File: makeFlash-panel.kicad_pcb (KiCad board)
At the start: 2 copper layers, 100.1 x 78.7 mm, 34 parts, among them Q1 2N3904, Q2 2N3904

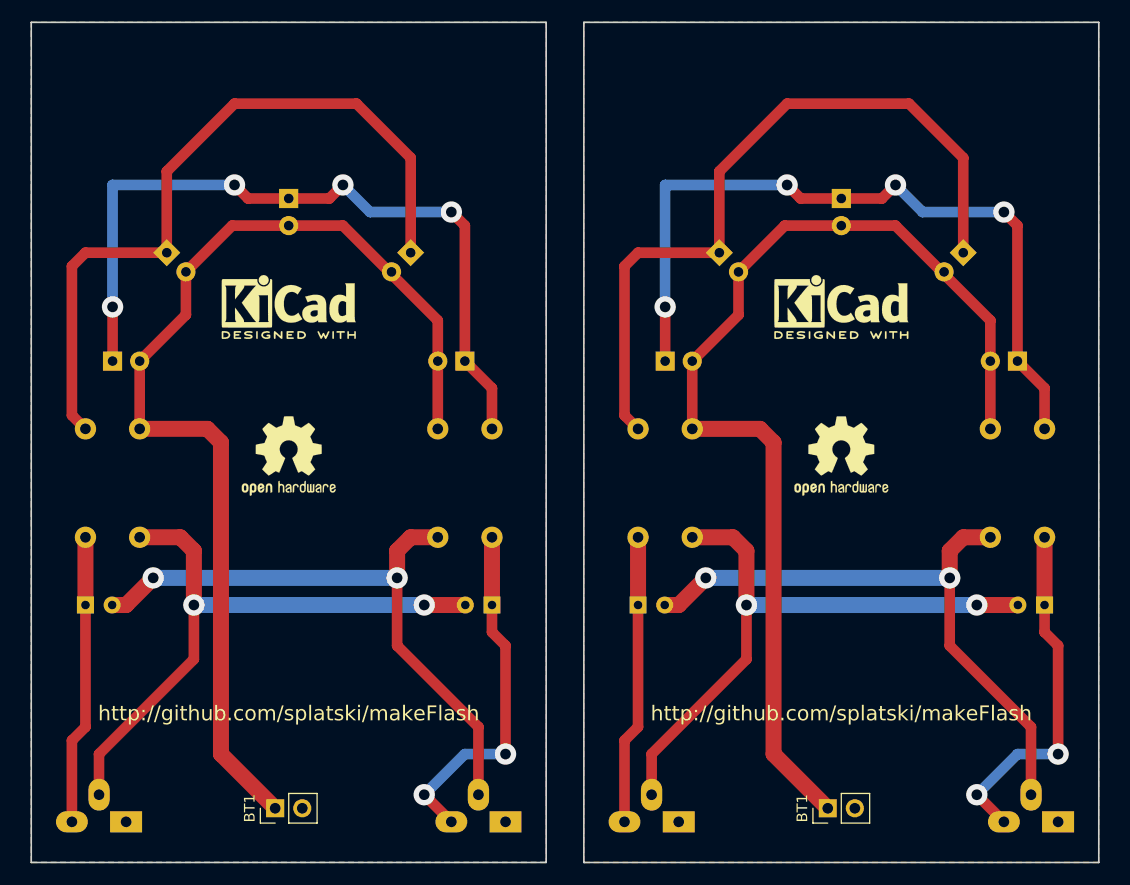
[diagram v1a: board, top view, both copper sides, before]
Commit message: slight reduction in size to definately fit within 100mm
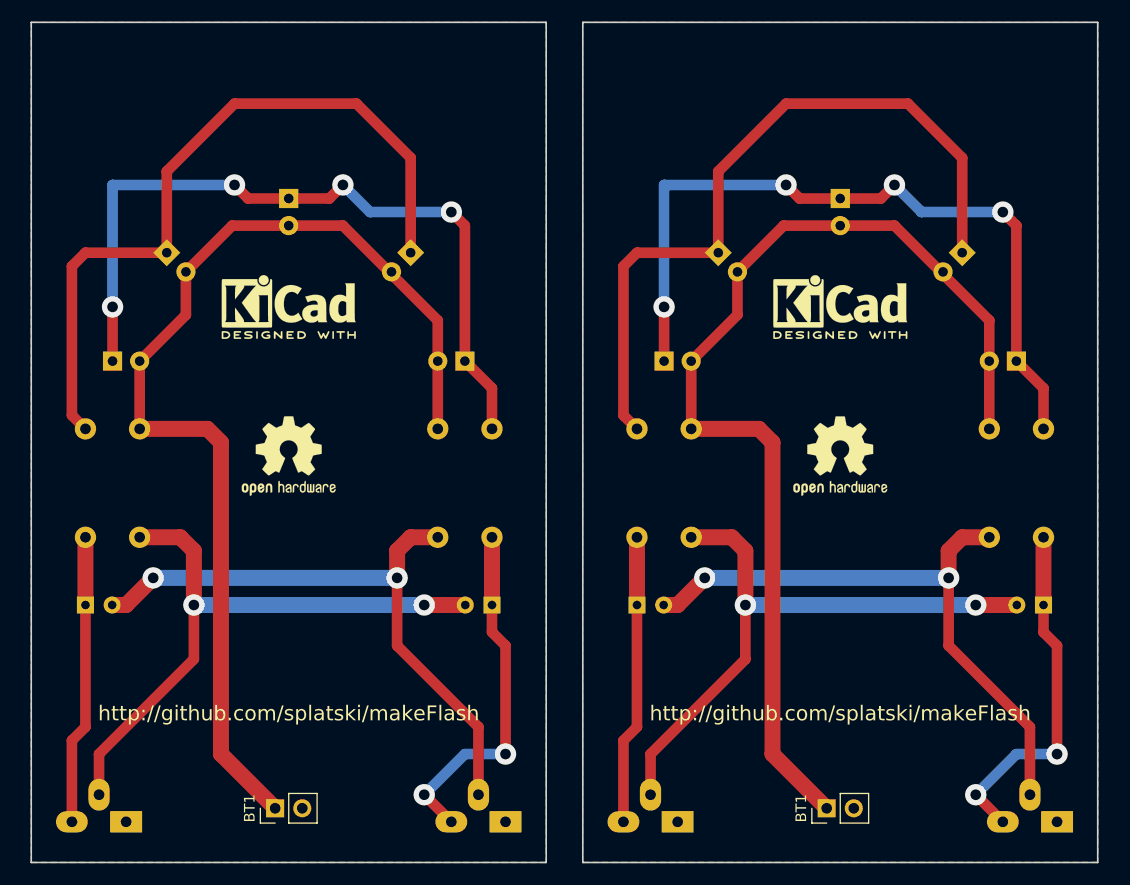
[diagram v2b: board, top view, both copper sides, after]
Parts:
- moved D3 0.10 mm to (136.8, 115.6)
- moved G*** 0.10 mm to (136.8, 133.3)
- moved KiCadLogo 0.10 mm to (136.8, 125.7)
- moved R4 0.10 mm to (150.8, 137.2)
- moved REF*** 0.10 mm to (136.8, 139.7)
- moved D1 0.10 mm to (120.3, 130.8)
- moved D2 0.10 mm to (125.4, 120.6)
- moved Q1 0.10 mm to (121.5, 174.0)
- moved BT1 0.10 mm to (135.5, 172.7)
- moved C1 0.10 mm to (117.7, 153.7)
- moved C2 0.10 mm to (155.8, 153.7)
- moved D4 0.10 mm to (148.2, 120.6)
- moved D5 0.10 mm to (153.3, 130.8)
- moved Q2 0.10 mm to (157.1, 174.0)
- moved R1 0.10 mm to (117.7, 137.2)
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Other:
- board size 100.1 x 78.7 mm -> 100 x 78.7 mm

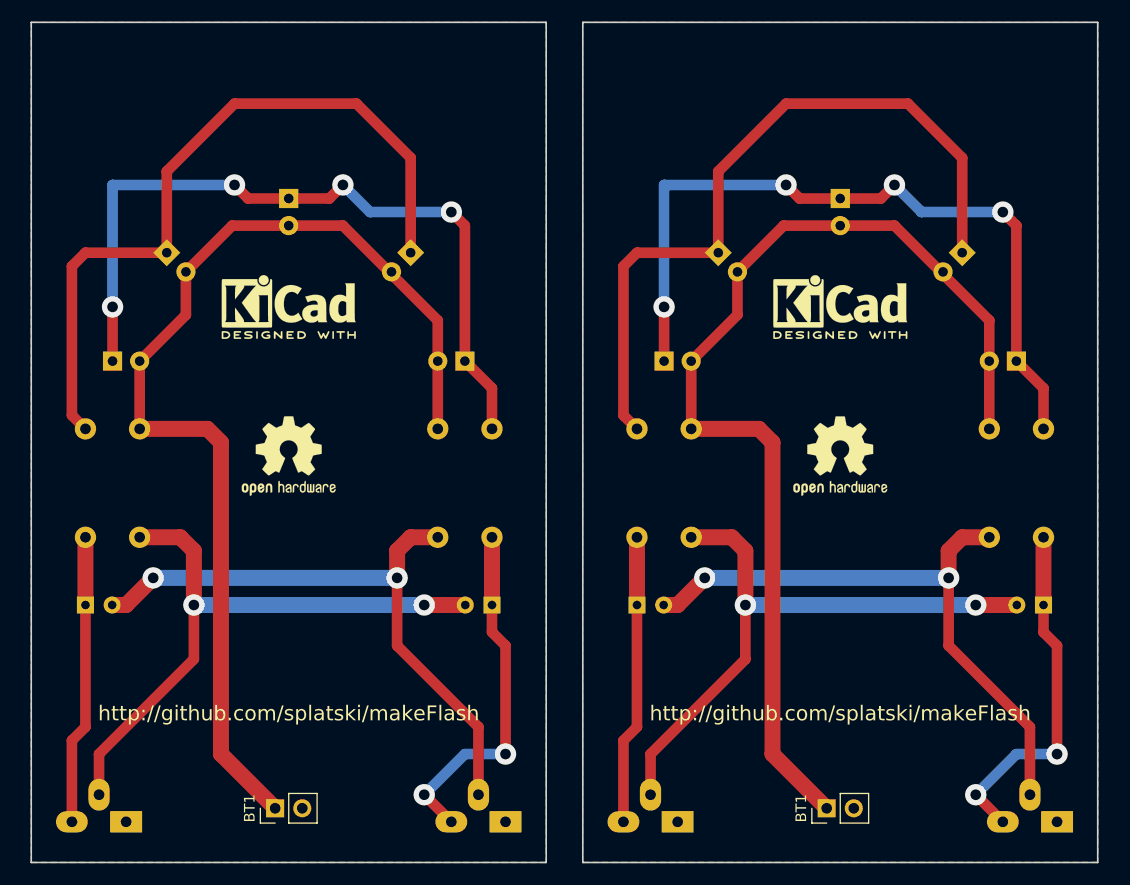
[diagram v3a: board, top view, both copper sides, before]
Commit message: fixed outline to cover board boards
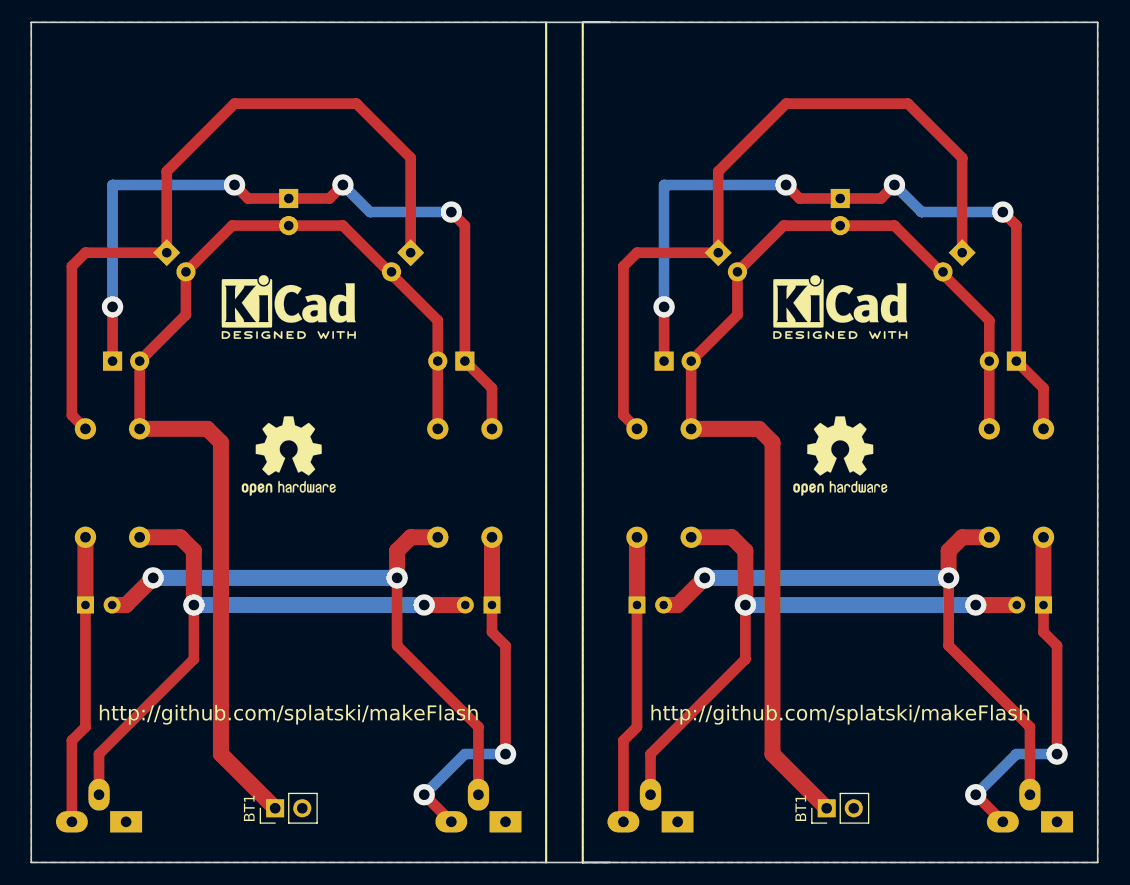
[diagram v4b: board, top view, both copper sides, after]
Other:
- outline, holes or cut-outs redrawn
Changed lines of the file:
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@@
     (area 60.886359 98.979019 160.987021 178.05484)
     (thickness 1.6)
-    (drawings 12)
+    (drawings 13)
     (tracks 152)
     (zones 0)
@@
       (xy -0.017575 -3.712307) (xy 0 -3.712308) (xy 0.139878 -3.712224)) (layer F.SilkS) (width 0.01))
   )
+  (gr_line (start 112.649 177.8) (end 112.7125 177.8) (angle 90) (layer F.SilkS) (width 0.2))
+  (gr_line (start 112.649 99.06) (end 112.649 177.8) (angle 90) (layer F.SilkS) (width 0.2))
+  (gr_line (start 109.22 177.8) (end 109.22 99.06) (angle 90) (layer F.SilkS) (width 0.2))
   (gr_text http://github.com/splatski/makeFlash (at 136.78202 163.82584) (layer F.SilkS)
     (effects (font (size 1.4 1.4) (thickness 0.3)))
   )
-  (gr_line (start 112.65202 99.05584) (end 112.65202 177.79584) (angle 90) (layer Edge.Cuts) (width 0.15))
   (gr_line (start 160.91202 99.05584) (end 112.65202 99.05584) (angle 90) (layer Edge.Cuts) (width 0.15))
   (gr_line (start 160.91202 177.79584) (end 160.91202 99.05584) (angle 90) (layer Edge.Cuts) (width 0.15))
@@
   )
   (gr_line (start 60.96136 99.05402) (end 60.96136 177.79402) (angle 90) (layer Edge.Cuts) (width 0.15))
-  (gr_line (start 109.22136 99.05402) (end 60.96136 99.05402) (angle 90) (layer Edge.Cuts) (width 0.15))
-  (gr_line (start 109.22136 177.79402) (end 109.22136 99.05402) (angle 90) (layer Edge.Cuts) (width 0.15))
-  (gr_line (start 60.96136 177.79402) (end 109.22136 177.79402) (angle 90) (layer Edge.Cuts) (width 0.15))
+  (gr_line (start 115.22136 99.05402) (end 60.96136 99.05402) (angle 90) (layer Edge.Cuts) (width 0.15))
+  (gr_line (start 60.96136 177.79402) (end 115.22136 177.79402) (angle 90) (layer Edge.Cuts) (width 0.15))
   (gr_text http://hobartmakers.com/ (at 85.09136 168.90402) (layer B.SilkS)
     (effects (font (size 1.5 1.5) (thickness 0.3)) (justify mirror))
